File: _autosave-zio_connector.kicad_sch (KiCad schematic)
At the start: 4 parts, among them CN10 Conn_02x17_Odd_Even, CN7 Conn_02x10_Odd_Even, CN8 Conn_02x08_Odd_Even, CN9 Conn_02x15_Odd_Even

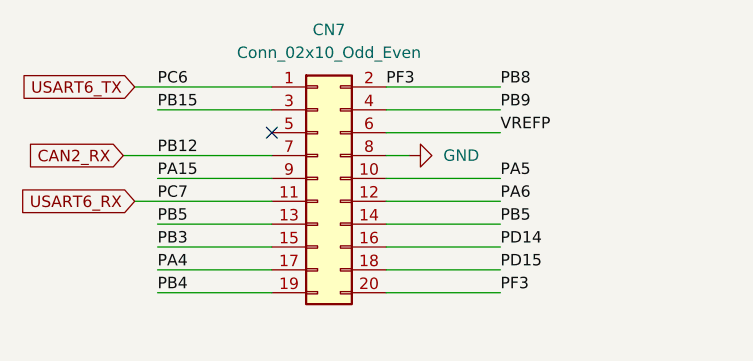
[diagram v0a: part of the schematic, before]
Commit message: add mapping for ADCs
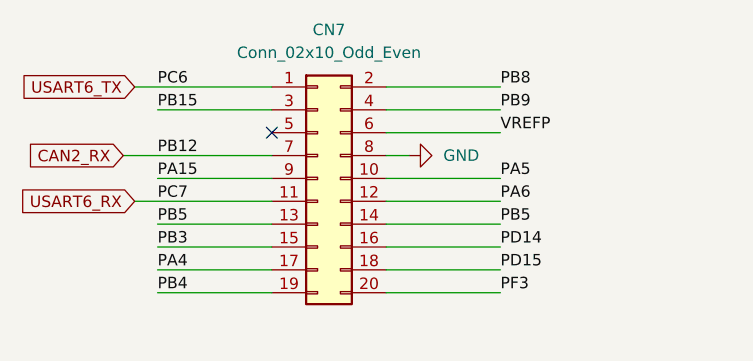
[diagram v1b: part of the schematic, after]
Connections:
- net PB8: no longer CN7.20 (Pin_20)
- new net PF3: CN7.20 (Pin_20)
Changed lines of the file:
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@@
-		)
-	)
-	(label "PF3"
-		(at 144.78 25.4 0)
-		(fields_autoplaced yes)
-		(effects
-			(font
-				(size 1.27 1.27)
-			)
-			(justify left bottom)
 		)
 	)
